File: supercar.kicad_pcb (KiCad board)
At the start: 2 copper layers, 63.5 x 48.9 mm, 54 parts, among them SW1 Power, U1 74HC283, U2 74HC574, U3 74HC154, U4 74HC574, U5 74HC86, U6 NE555D

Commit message: Update schematics
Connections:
- RN1 pad 4: +3.3V -> +3V3
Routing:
- net +3V3: track 269.2 -> 272.5 mm, vias 5 -> 6
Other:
- board text added: "Rev. 2"
- board text removed: "Rev. 1"

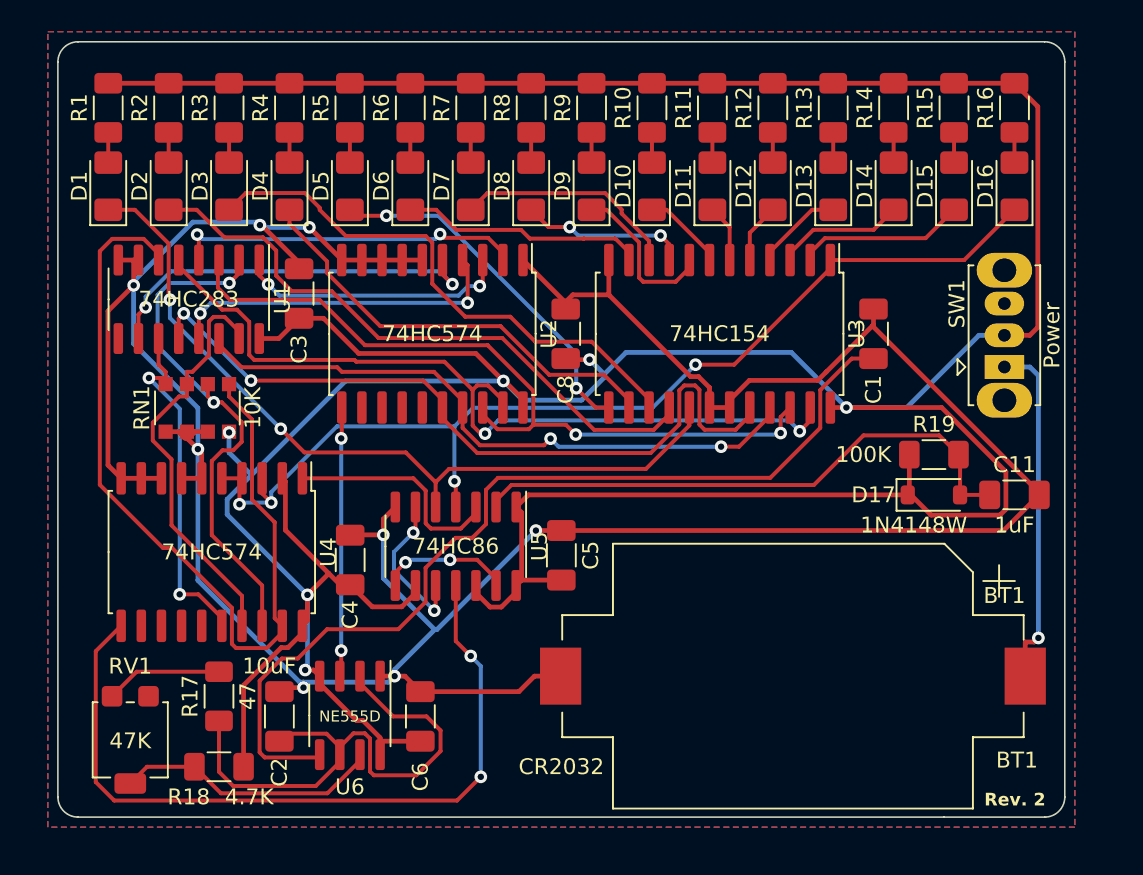
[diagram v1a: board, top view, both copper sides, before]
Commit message: Use a single resistor, reduce the size of the PCB
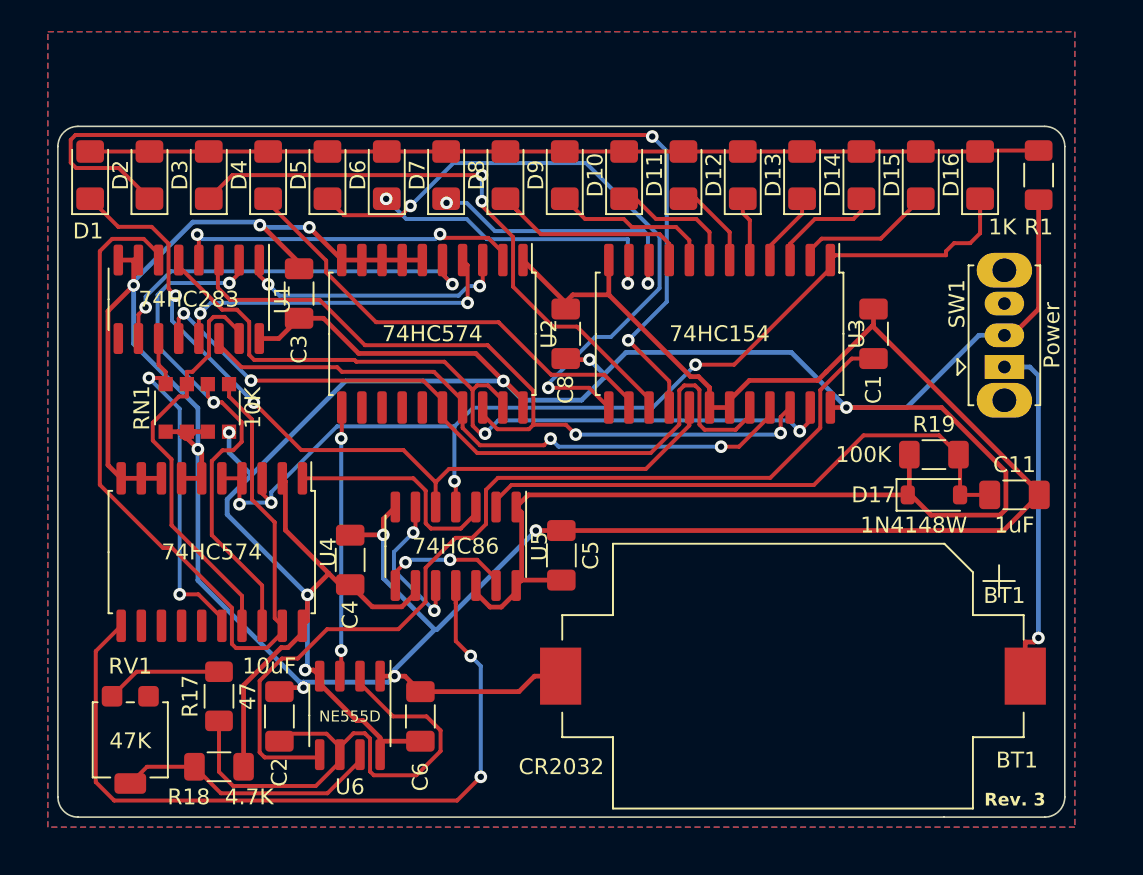
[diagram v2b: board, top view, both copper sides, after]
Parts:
- removed R10, R11, R12, R13, R14, R15, R16, R2, R3, R4, R5, R6, R7, R8, R9: 470, Resistor_SMD:R_1206_3216Metric_Pad1.30x1.75mm_HandSolder
- R1: value 470 -> 1K
- moved R1 58.8 mm to (140.0, 47.8), turned to -90 degrees
- moved D16 2.28 mm to (136.3, 47.8)
- moved D15 2.21 mm to (132.5, 47.8)
- moved D14 2.15 mm to (128.8, 47.8)
- moved D13 2.08 mm to (125.0, 47.8)
- moved D12 2.02 mm to (121.3, 47.8)
- moved D11 1.96 mm to (117.6, 47.8)
- moved D10 1.89 mm to (113.8, 47.8)
- moved D9 1.83 mm to (110.1, 47.8)
- moved D8 1.77 mm to (106.3, 47.8)
- moved D7 1.70 mm to (102.6, 47.8)
- moved D6 1.64 mm to (98.8, 47.8)
- moved D5 1.58 mm to (95.1, 47.8)
- moved D4 1.52 mm to (91.4, 47.8)
- moved D3 1.46 mm to (87.6, 47.8)
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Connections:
- D10 pad 2: Net-(D10-A) -> Net-(D1-A)
- D11 pad 2: Net-(D11-A) -> Net-(D1-A)
- D12 pad 2: Net-(D12-A) -> Net-(D1-A)
- D13 pad 2: Net-(D13-A) -> Net-(D1-A)
- D14 pad 2: Net-(D14-A) -> Net-(D1-A)
- D15 pad 2: Net-(D15-A) -> Net-(D1-A)
- D16 pad 2: Net-(D16-A) -> Net-(D1-A)
- D2 pad 2: Net-(D2-A) -> Net-(D1-A)
- D3 pad 2: Net-(D3-A) -> Net-(D1-A)
- D4 pad 2: Net-(D4-A) -> Net-(D1-A)
- D5 pad 2: Net-(D5-A) -> Net-(D1-A)
- D6 pad 2: Net-(D6-A) -> Net-(D1-A)
- D7 pad 2: Net-(D7-A) -> Net-(D1-A)
- D8 pad 2: Net-(D8-A) -> Net-(D1-A)
- D9 pad 2: Net-(D9-A) -> Net-(D1-A)
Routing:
- net +3V3: track 272.5 -> 206.8 mm
- net Net-(D1-A): track 1.91 -> 59.8 mm
- net Net-(D2-K): track 39.1 -> 63.7 mm, vias 0 -> 2
- net Net-(D5-K): track 22.8 -> 42.0 mm
- net Net-(D6-K): track 15.4 -> 20.6 mm, vias 0 -> 2
- net Net-(D7-K): track 14.3 -> 18.4 mm, vias 0 -> 2
- net Net-(D3-K): track 34.4 -> 37.7 mm, vias 0 -> 2
- net Net-(D8-K): track 10.6 -> 13.8 mm, vias 2 -> 0
- net Net-(D10-K): track 5.22 -> 8.02 mm
- net /LAST_BIT: track 50.6 -> 53.1 mm
- net Net-(D11-K): track 3.62 -> 5.55 mm
- net Net-(D9-A): track 1.91 -> 0.00 mm
- net Net-(D8-A): track 1.91 -> 0.00 mm
- net Net-(D7-A): track 1.91 -> 0.00 mm
- net Net-(D6-A): track 1.91 -> 0.00 mm
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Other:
- board size 63.5 x 48.9 mm -> 63.5 x 43.6 mm
- board text added: "Rev. 3"
- board text removed: "Rev. 2"

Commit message: Fix cap position in rev3
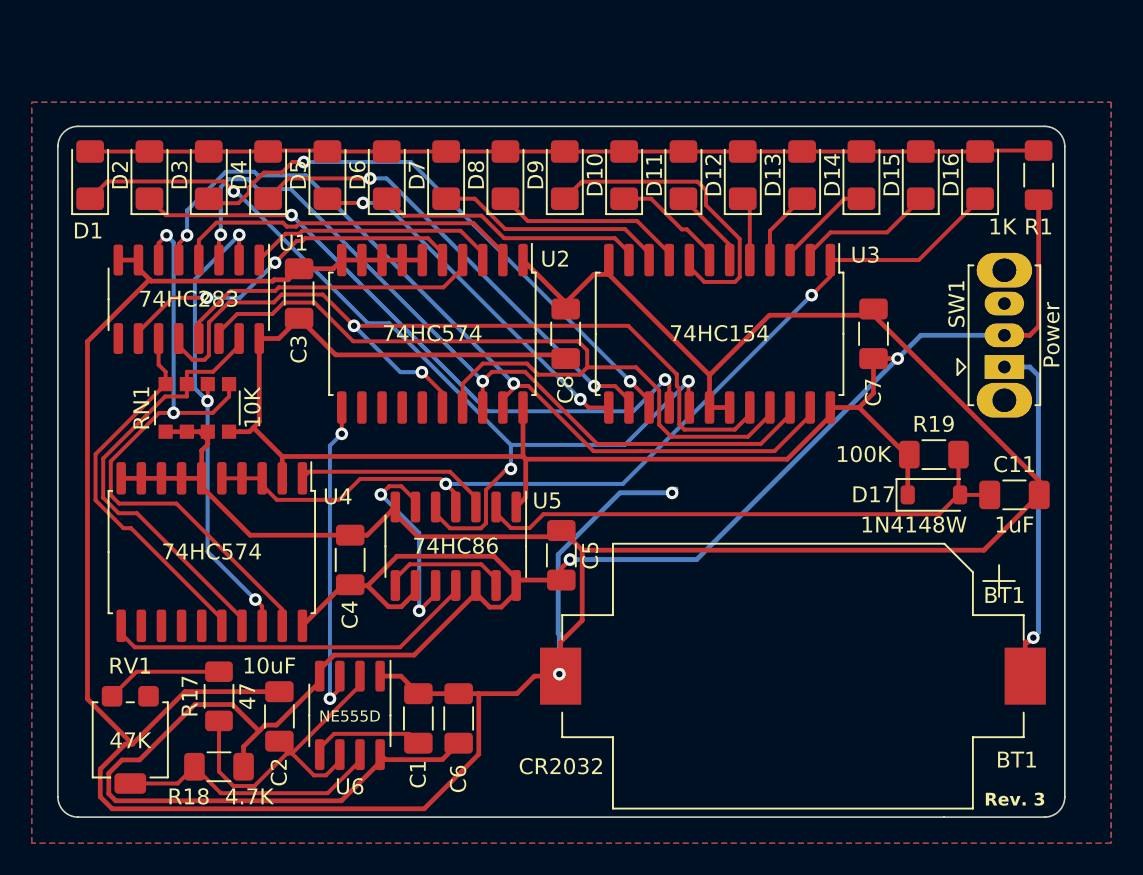
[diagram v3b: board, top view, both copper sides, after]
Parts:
- added C7: 100nF, Capacitor_SMD:C_1206_3216Metric_Pad1.33x1.80mm_HandSolder, F.Cu at (129.5, 57.8)
- moved C1 37.6 mm to (100.8, 82.0)
- moved C6 2.42 mm to (103.4, 82.0)
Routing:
- net Net-(U6-CV): track 59.6 -> 7.25 mm
- net GND: track 206.0 -> 253.0 mm, vias 8 -> 2
- net Net-(U4-Cp): track 49.7 -> 23.8 mm, vias 2 -> 0
- net Net-(D2-K): track 63.7 -> 40.8 mm
- net Net-(D5-K): track 42.0 -> 23.2 mm
- net Net-(RN1-R4.2): track 54.1 -> 40.1 mm, vias 0 -> 2
- net Net-(U6-THR): track 34.9 -> 21.0 mm
- net +3V3: track 206.8 -> 219.4 mm, vias 6 -> 2
- net Net-(U1-A3): track 40.5 -> 52.7 mm, vias 2 -> 0
- net Net-(D9-K): track 10.2 -> 20.1 mm
- net /FIRST_BIT: track 68.5 -> 59.1 mm, vias 4 -> 2
- net Net-(U1-A4): track 48.1 -> 54.2 mm
- net /LAST_BIT: track 53.1 -> 58.3 mm, vias 2 -> 3
- net Net-(D7-K): track 18.4 -> 14.7 mm, vias 2 -> 0
- net Net-(D6-K): track 20.6 -> 17.2 mm, vias 2 -> 0
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
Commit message: Reroute rev_3
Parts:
- RN1: footprint Resistor_SMD:R_Array_Convex_4x1206 -> Resistor_SMD:R_Array_Convex_4x0612
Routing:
- net GND: track 253.0 -> 218.8 mm, vias 2 -> 6
- net Net-(RN1-R3.2): track 30.2 -> 58.2 mm, vias 3 -> 2
- net +3V3: track 219.4 -> 238.2 mm, vias 2 -> 3
- net Net-(D8-K): track 12.2 -> 25.1 mm
- net Net-(U1-A3): track 52.7 -> 41.3 mm, vias 0 -> 2
- net Net-(D9-K): track 20.1 -> 9.76 mm
- net Net-(U1-A4): track 54.2 -> 46.2 mm, vias 2 -> 0
- net /LAST_BIT: track 58.3 -> 52.3 mm
- net Net-(RN1-R4.2): track 40.1 -> 35.1 mm, vias 2 -> 3
- net Net-(U5-Pad10): track 13.6 -> 8.77 mm
- net Net-(U1-A2): track 51.0 -> 46.5 mm
- net Net-(U4-Cp): track 23.8 -> 28.3 mm
- net Net-(U1-S3): track 19.6 -> 22.9 mm, vias 0 -> 2
- net Net-(D3-K): track 35.8 -> 39.1 mm
- net /CLK: track 20.3 -> 18.1 mm
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
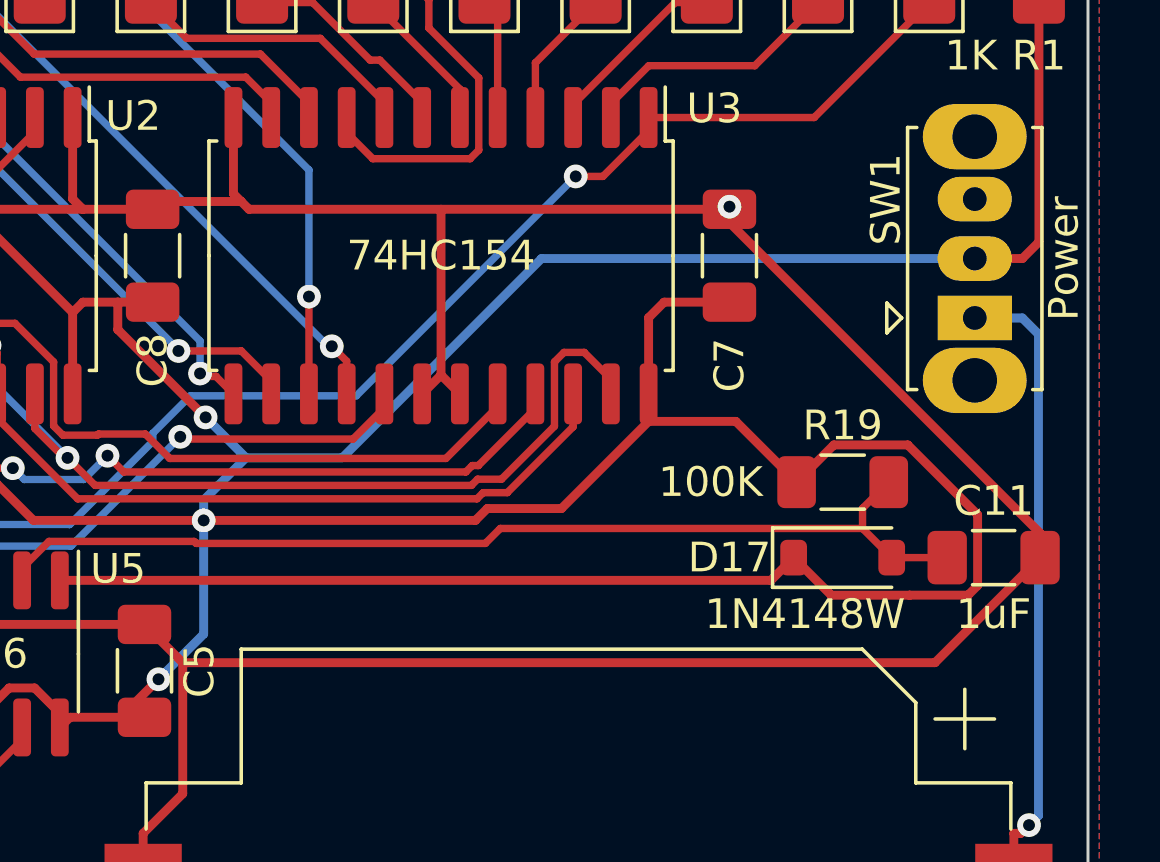
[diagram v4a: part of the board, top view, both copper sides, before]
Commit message: add 47uf cap as buffer to battery
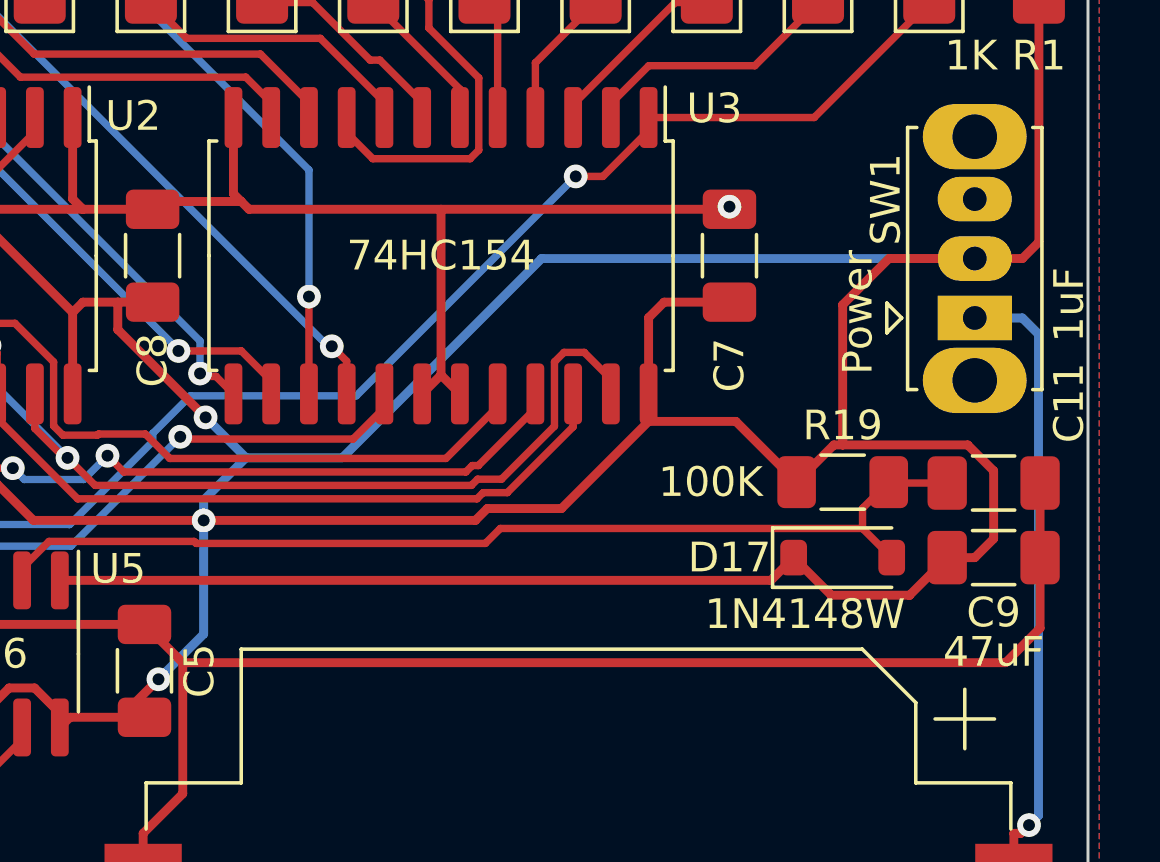
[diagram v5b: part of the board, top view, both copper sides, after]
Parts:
- added C9: 47uF, Capacitor_SMD:C_1206_3216Metric_Pad1.33x1.80mm_HandSolder, F.Cu at (138.4, 67.9)
- moved C11 2.51 mm to (138.4, 65.4)
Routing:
- net GND: track 218.8 -> 206.8 mm
- net +3V3: track 238.2 -> 249.0 mm

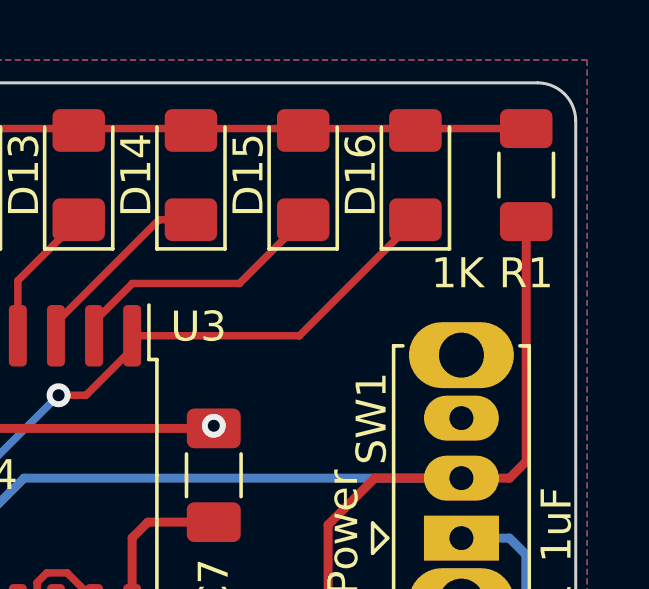
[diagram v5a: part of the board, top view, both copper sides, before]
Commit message: Resistor led now 2.2K
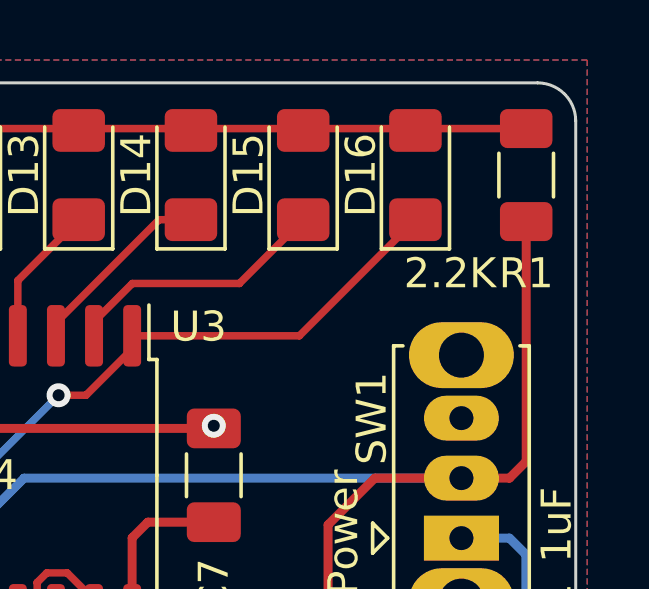
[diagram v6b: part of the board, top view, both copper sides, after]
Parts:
- R1: value 1K -> 2.2K
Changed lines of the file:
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@@
         (effects (font (size 1 1) (thickness 0.15)))
     )
-    (fp_text value "1K" (at 3.276 2.286 -180) (layer "F.SilkS")
+    (fp_text value "2.2K" (at 3.276 2.54 -180) (layer "F.SilkS")
         (effects (font (size 1 1) (thickness 0.15)))
     )
